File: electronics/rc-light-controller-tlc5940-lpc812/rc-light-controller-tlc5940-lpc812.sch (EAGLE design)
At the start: 38 parts, among them U2 TLC5940PWP

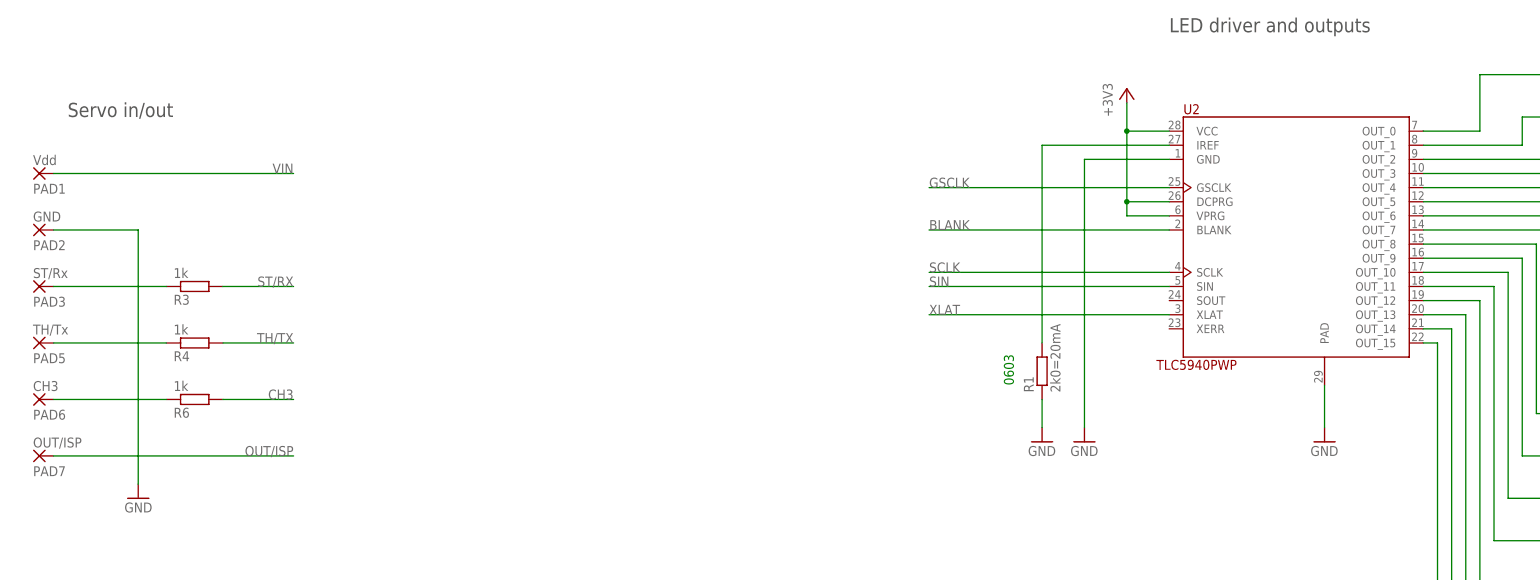
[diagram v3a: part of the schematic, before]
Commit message: Add protection resistor to OUT/ISP line
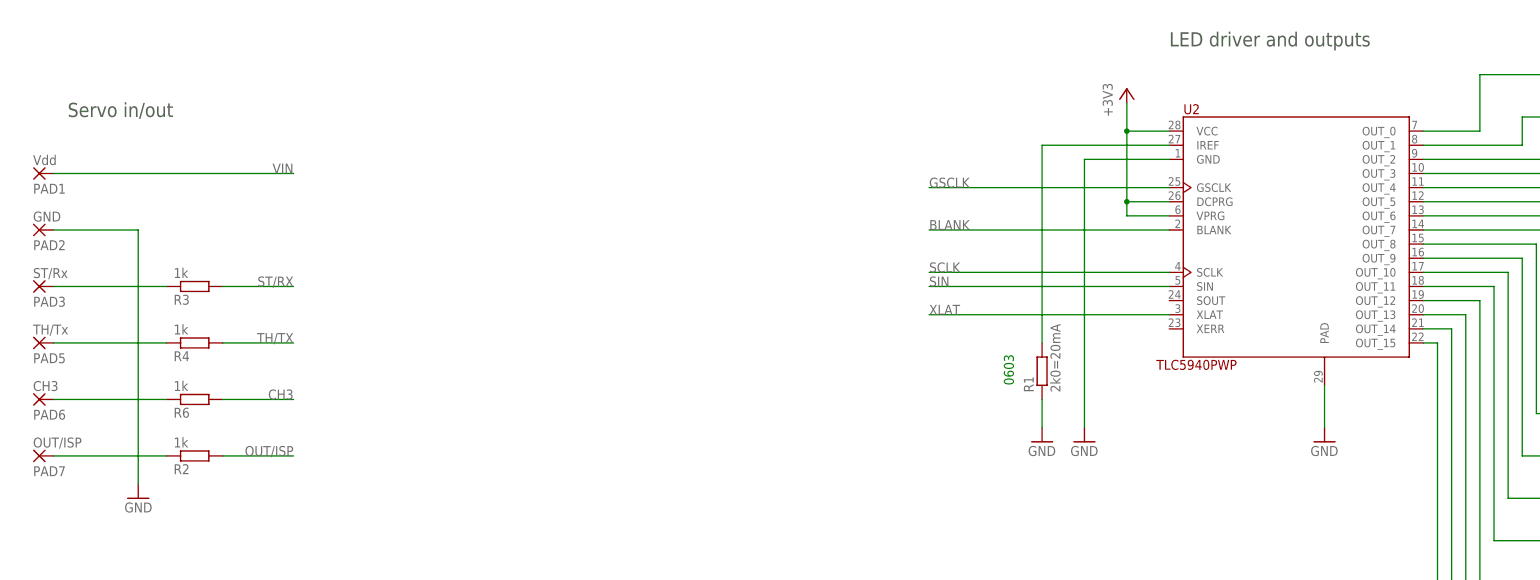
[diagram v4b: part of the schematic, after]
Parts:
- added R2: 1k, rcl:R-EU_R0603
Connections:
- new net N$2: PAD7.P, R2.1
- net OUT/ISP: now also R2.2; no longer PAD7.P
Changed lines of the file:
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@@
 <part name="GND9" library="supply1" deviceset="GND" device=""/>
 <part name="FRAME1" library="frames" deviceset="A3L-LOC" device=""/>
+<part name="R2" library="rcl" deviceset="R-EU_" device="R0603" value="1k"/>
 </parts>
 <sheets>
@@
 PIO0_11 ( 7)   Open drain</text>
 <text x="40.64" y="233.68" size="2.54" layer="97">Servo in/out</text>
-<text x="238.76" y="248.92" size="2.54" layer="97">LED driver and outputs</text>
+<text x="238.76" y="246.38" size="2.54" layer="97">LED driver and outputs</text>
 <text x="43.18" y="71.12" size="2.54" layer="97">Voltage regulator</text>
 <text x="160.02" y="139.7" size="2.54" layer="97">Microcontroller</text>
@@
 <attribute name="SHEET" x="357.505" y="5.08" size="2.54" layer="94" font="vector"/>
 </instance>
+<instance part="R2" gate="G$1" x="63.5" y="172.72" rot="MR180"/>
 </instances>
 <busses>
@@
 <net name="OUT/ISP" class="0">
 <segment>
-<wire x1="81.28" y1="172.72" x2="38.1" y2="172.72" width="0.1524" layer="91"/>
-<pinref part="PAD7" gate="G$1" pin="P"/>
-<label x="81.28" y="172.72" size="1.778" layer="95" rot="MR0"/>
-</segment>
-<segment>
 <wire x1="223.52" y1="116.84" x2="208.28" y2="116.84" width="0.1524" layer="91"/>
 <pinref part="U$2" gate="G$1" pin="PIO0_12"/>
 <label x="218.44" y="116.84" size="1.778" layer="95"/>
 </segment>
+<segment>
+<pinref part="R2" gate="G$1" pin="2"/>
+<wire x1="81.28" y1="172.72" x2="68.58" y2="172.72" width="0.1524" layer="91"/>
+<label x="81.28" y="172.72" size="1.778" layer="95" rot="MR0"/>
+</segment>
 </net>
 <net name="N$1" class="0">
@@
 </segment>
 </net>
+<net name="N$2" class="0">
+<segment>
+<pinref part="PAD7" gate="G$1" pin="P"/>
+<pinref part="R2" gate="G$1" pin="1"/>
+<wire x1="38.1" y1="172.72" x2="58.42" y2="172.72" width="0.1524" layer="91"/>
+</segment>
+</net>

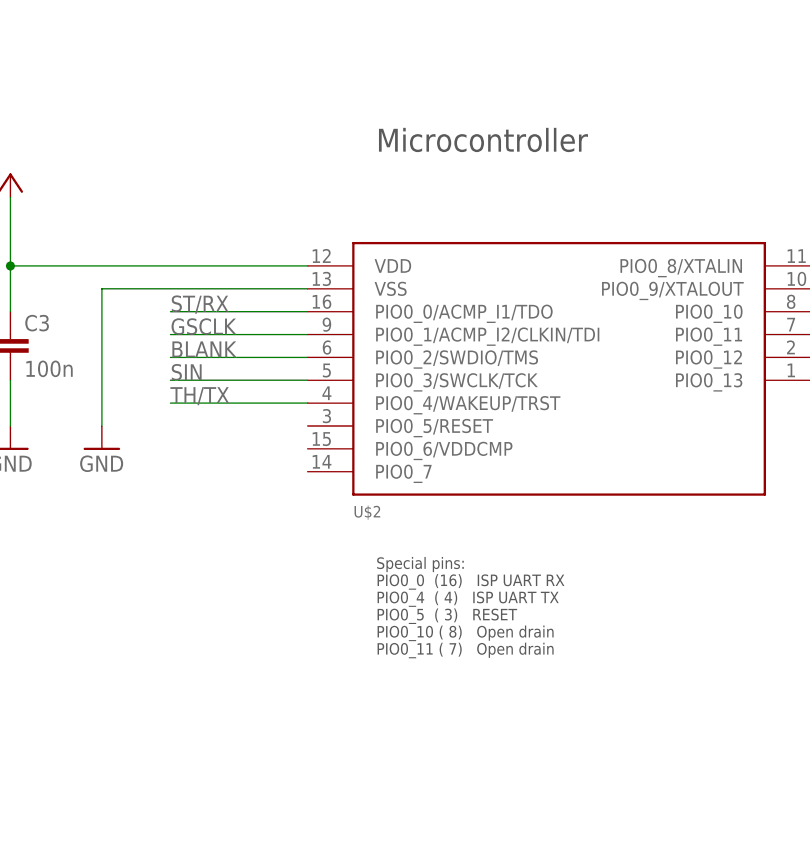
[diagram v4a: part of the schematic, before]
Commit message: Add test points for SWDIO and SWCLK
Apparently useful if one accidentally disables the bootloader
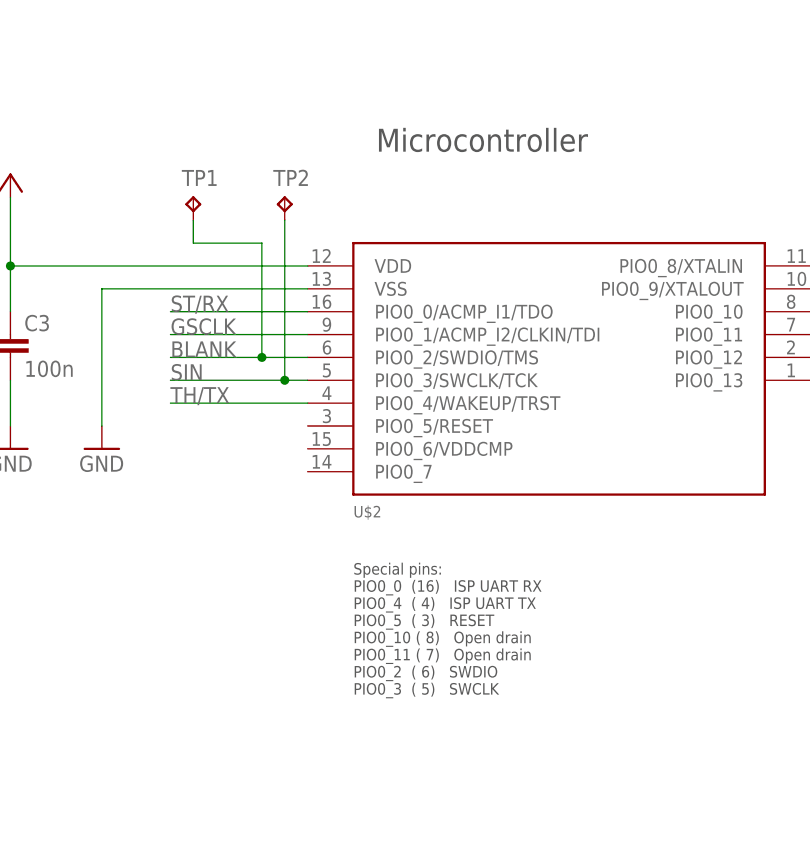
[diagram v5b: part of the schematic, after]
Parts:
- added TP1: SWDIO, testpad:TPTP10R
- added TP2: SWCLK, testpad:TPTP10R
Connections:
- net BLANK: now also TP1.TP
- net SIN: now also TP2.TP
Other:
- note added: "Special pins: PIO0_0 (16) ISP UART RX PIO0_4 ( 4) ISP UART TX PIO0_5 ( 3) RESET PIO0_10 ( 8) Open drain PIO0_11 ( 7) Open drain PIO0_2 ( 6) SWDIO PIO0_3 ( 5) SWCLK"
- note removed: "Special pins: PIO0_0 (16) ISP UART RX PIO0_4 ( 4) ISP UART TX PIO0_5 ( 3) RESET PIO0_10 ( 8) Open drain PIO0_11 ( 7) Open drain"
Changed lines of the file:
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@@
 <grid distance="0.1" unitdist="inch" unit="inch" style="lines" multiple="1" display="no" altdistance="0.01" altunitdist="inch" altunit="inch"/>
 <layers>
-<layer number="1" name="Top" color="4" fill="1" visible="no" active="no"/>
-<layer number="16" name="Bottom" color="1" fill="1" visible="no" active="no"/>
-<layer number="17" name="Pads" color="2" fill="1" visible="no" active="no"/>
-<layer number="18" name="Vias" color="2" fill="1" visible="no" active="no"/>
-<layer number="19" name="Unrouted" color="6" fill="1" visible="no" active="no"/>
-<layer number="20" name="Dimension" color="15" fill="1" visible="no" active="no"/>
-<layer number="21" name="tPlace" color="7" fill="1" visible="no" active="no"/>
-<layer number="22" name="bPlace" color="7" fill="1" visible="no" active="no"/>
-<layer number="23" name="tOrigins" color="15" fill="1" visible="no" active="no"/>
-<layer number="24" name="bOrigins" color="15" fill="1" visible="no" active="no"/>
-<layer number="25" name="tNames" color="7" fill="1" visible="no" active="no"/>
-<layer number="26" name="bNames" color="7" fill="1" visible="no" active="no"/>
-<layer number="27" name="tValues" color="7" fill="1" visible="no" active="no"/>
-<layer number="28" name="bValues" color="7" fill="1" visible="no" active="no"/>
+<layer number="1" name="Top" color="4" fill="1" visible="yes" active="no"/>
+<layer number="16" name="Bottom" color="1" fill="1" visible="yes" active="no"/>
+<layer number="17" name="Pads" color="2" fill="1" visible="yes" active="no"/>
+<layer number="18" name="Vias" color="2" fill="1" visible="yes" active="no"/>
+<layer number="19" name="Unrouted" color="6" fill="1" visible="yes" active="no"/>
+<layer number="20" name="Dimension" color="15" fill="1" visible="yes" active="no"/>
+<layer number="21" name="tPlace" color="7" fill="1" visible="yes" active="no"/>
+<layer number="22" name="bPlace" color="7" fill="1" visible="yes" active="no"/>
+<layer number="23" name="tOrigins" color="15" fill="1" visible="yes" active="no"/>
+<layer number="24" name="bOrigins" color="15" fill="1" visible="yes" active="no"/>
+<layer number="25" name="tNames" color="7" fill="1" visible="yes" active="no"/>
+<layer number="26" name="bNames" color="7" fill="1" visible="yes" active="no"/>
+<layer number="27" name="tValues" color="7" fill="1" visible="yes" active="no"/>
+<layer number="28" name="bValues" color="7" fill="1" visible="yes" active="no"/>
 <layer number="29" name="tStop" color="7" fill="3" visible="no" active="no"/>
 <layer number="30" name="bStop" color="7" fill="6" visible="no" active="no"/>
@@
 <layer number="35" name="tGlue" color="7" fill="4" visible="no" active="no"/>
 <layer number="36" name="bGlue" color="7" fill="5" visible="no" active="no"/>
-<layer number="37" name="tTest" color="7" fill="1" visible="no" active="no"/>
-<layer number="38" name="bTest" color="7" fill="1" visible="no" active="no"/>
+<layer number="37" name="tTest" color="7" fill="1" visible="yes" active="no"/>
+<layer number="38" name="bTest" color="7" fill="1" visible="yes" active="no"/>
 <layer number="39" name="tKeepout" color="4" fill="11" visible="no" active="no"/>
 <layer number="40" name="bKeepout" color="1" fill="11" visible="no" active="no"/>
@@
 <layer number="44" name="Drills" color="7" fill="1" visible="no" active="no"/>
 <layer number="45" name="Holes" color="7" fill="1" visible="no" active="no"/>
-<layer number="46" name="Milling" color="3" fill="1" visible="no" active="no"/>
-<layer number="47" name="Measures" color="7" fill="1" visible="no" active="no"/>
-<layer number="48" name="Document" color="7" fill="1" visible="no" active="no"/>
-<layer number="49" name="Reference" color="7" fill="1" visible="no" active="no"/>
-<layer number="50" name="dxf" color="7" fill="1" visible="no" active="no"/>
-<layer number="51" name="tDocu" color="7" fill="1" visible="no" active="no"/>
-<layer number="52" name="bDocu" color="7" fill="1" visible="no" active="no"/>
-<layer number="53" name="tGND_GNDA" color="7" fill="9" visible="no" active="no"/>
-<layer number="54" name="bGND_GNDA" color="1" fill="9" visible="no" active="no"/>
-<layer number="56" name="wert" color="7" fill="1" visible="no" active="no"/>
+<layer number="46" name="Milling" color="3" fill="1" visible="yes" active="no"/>
+<layer number="47" name="Measures" color="7" fill="1" visible="yes" active="no"/>
+<layer number="48" name="Document" color="7" fill="1" visible="yes" active="no"/>
+<layer number="49" name="Reference" color="7" fill="1" visible="yes" active="no"/>
+<layer number="50" name="dxf" color="7" fill="1" visible="yes" active="no"/>
+<layer number="51" name="tDocu" color="7" fill="1" visible="yes" active="no"/>
+<layer number="52" name="bDocu" color="7" fill="1" visible="yes" active="no"/>
+<layer number="53" name="tGND_GNDA" color="7" fill="9" visible="yes" active="no"/>
+<layer number="54" name="bGND_GNDA" color="1" fill="9" visible="yes" active="no"/>
+<layer number="56" name="wert" color="7" fill="1" visible="yes" active="no"/>
 <layer number="91" name="Nets" color="2" fill="1" visible="yes" active="yes"/>
 <layer number="92" name="Busses" color="1" fill="1" visible="no" active="yes"/>
@@
 <part name="FRAME1" library="frames" deviceset="A3L-LOC" device=""/>
 <part name="R2" library="rcl" deviceset="R-EU_" device="R0603" value="1k"/>
+<part name="TP1" library="testpad" deviceset="TP" device="TP10R" value="SWDIO"/>
+<part name="TP2" library="testpad" deviceset="TP" device="TP10R" value="SWCLK"/>
 </parts>
 <sheets>
@@
 <plain>
 <text x="210.82" y="185.42" size="1.778" layer="91" rot="R90">0603</text>
-<text x="160.02" y="83.82" size="1.27" layer="97">Special pins:
+<text x="157.48" y="93.98" size="1.27" layer="97" align="top-left">Special pins:
 PIO0_0  (16)   ISP UART RX
 PIO0_4  ( 4)   ISP UART TX
 PIO0_5  ( 3)   RESET
 PIO0_10 ( 8)   Open drain
-PIO0_11 ( 7)   Open drain</text>
+PIO0_11 ( 7)   Open drain
+PIO0_2  ( 6)   SWDIO
+PIO0_3  ( 5)   SWCLK</text>
 <text x="40.64" y="233.68" size="2.54" layer="97">Servo in/out</text>
 <text x="238.76" y="246.38" size="2.54" layer="97">LED driver and outputs</text>
@@
 </instance>
 <instance part="R2" gate="G$1" x="63.5" y="172.72" rot="MR180"/>
+<instance part="TP1" gate="G$1" x="139.7" y="134.62"/>
+<instance part="TP2" gate="G$1" x="149.86" y="134.62"/>
 </instances>
 <busses>
@@
 <segment>
 <pinref part="U$2" gate="G$1" pin="PIO0_3/SWCLK/TCK"/>
-<wire x1="152.4" y1="114.3" x2="137.16" y2="114.3" width="0.1524" layer="91"/>
+<wire x1="152.4" y1="114.3" x2="149.86" y2="114.3" width="0.1524" layer="91"/>
 <label x="137.16" y="114.3" size="1.778" layer="95"/>
+<wire x1="149.86" y1="114.3" x2="137.16" y2="114.3" width="0.1524" layer="91"/>
+<wire x1="149.86" y1="114.3" x2="149.86" y2="132.08" width="0.1524" layer="91"/>
+<junction x="149.86" y="114.3"/>
+<pinref part="TP2" gate="G$1" pin="TP"/>
 </segment>
 </net>
@@
 <segment>
 <pinref part="U$2" gate="G$1" pin="PIO0_2/SWDIO/TMS"/>
-<wire x1="152.4" y1="116.84" x2="137.16" y2="116.84" width="0.1524" layer="91"/>
+<wire x1="152.4" y1="116.84" x2="147.32" y2="116.84" width="0.1524" layer="91"/>
 <label x="137.16" y="116.84" size="1.778" layer="95"/>
-</segment>
-</net>
+<wire x1="147.32" y1="116.84" x2="137.16" y2="116.84" width="0.1524" layer="91"/>
+<wire x1="147.32" y1="116.84" x2="147.32" y2="129.54" width="0.1524" layer="91"/>
+<junction x="147.32" y="116.84"/>
+<pinref part="TP1" gate="G$1" pin="TP"/>
+<wire x1="147.32" y1="129.54" x2="139.7" y2="129.54" width="0.1524" layer="91"/>
+<wire x1="139.7" y1="129.54" x2="139.7" y2="132.08" width="0.1524" layer="91"/>
+</segment>
+</net>
